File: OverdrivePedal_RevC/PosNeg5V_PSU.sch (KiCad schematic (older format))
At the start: 25 parts, among them U11 TPS60400, U3 TPS60400, U7 SE8233X2, U8 SE8250X2

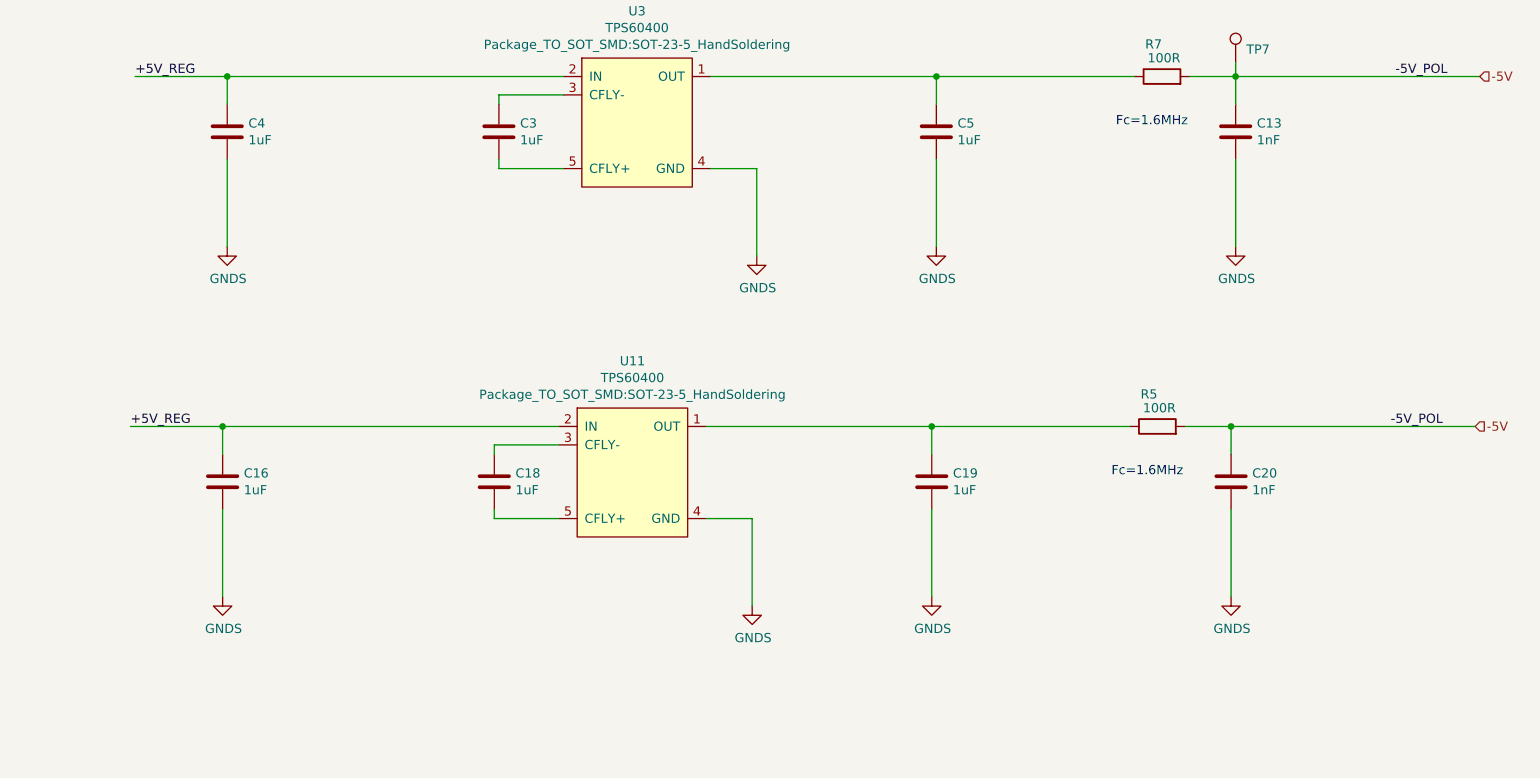
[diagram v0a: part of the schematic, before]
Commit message: updated revc
- Switch PC15 to PA9 for FX_ENABLE
- connected BOOT0 to GND
- Removed U11 charge pump (not required/causing oscillation)
- lowered U3 charge pump LP filter cuttoff to 1.6KHz
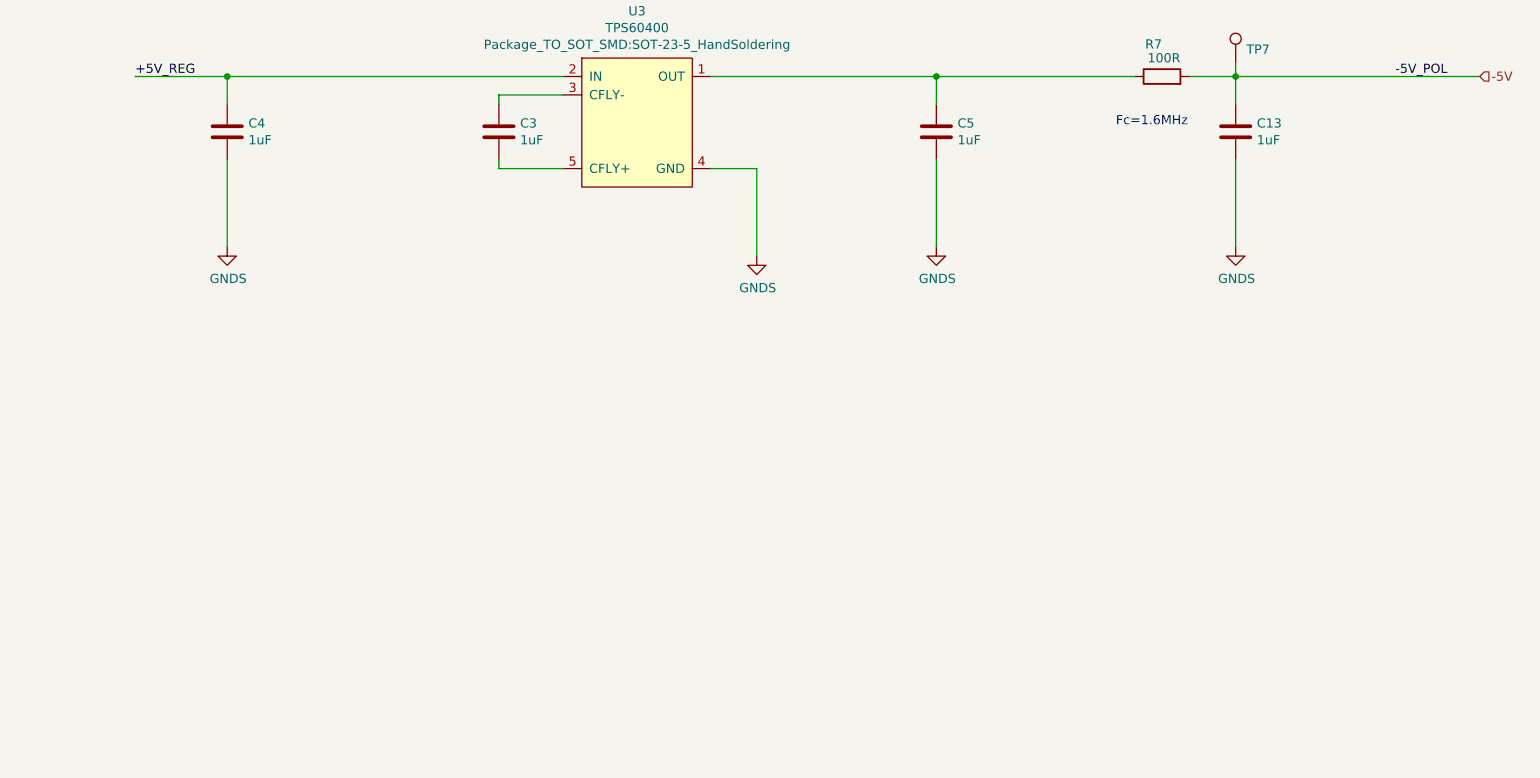
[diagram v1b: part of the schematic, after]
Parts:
- removed C16, C18, C19: 1uF, Capacitor_SMD:C_0402_1005Metric, symbol Device:C
- removed C20: 1nF, Capacitor_SMD:C_0402_1005Metric, symbol Device:C
- removed R5: 100R, Resistor_SMD:R_0402_1005Metric, symbol Device:R
- removed U11: TPS60400, Package_TO_SOT_SMD:SOT-23-5_HandSoldering, symbol TPS6040x:TPS60400
- C13: value 1nF -> 1uF
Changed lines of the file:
@@
 Title "Power Supply"
 Date "2020-03-29"
-Rev "RevB"
+Rev "RevC"
 Comp ""
 Comment1 "U11 may be omitted if U3 can provide enough -5V current"
@@
 AR Path="/5E6A8284/5E8237A8" Ref="C?"  Part="1"
 F 0 "C13" H 10665 5996 50  0000 L CNN
-F 1 "1nF" H 10665 5905 50  0000 L CNN
+F 1 "1uF" H 10665 5905 50  0000 L CNN
 F 2 "Capacitor_SMD:C_0402_1005Metric" H 10588 5800 50  0001 C CNN
 F 3 "~" H 10550 5950 50  0001 C CNN
@@
 -5V
 $Comp
-L power:GNDS #PWR015
-U 1 1 5E82512E
-P 7925 8525
-AR Path="/5E6165F4/5E82512E" Ref="#PWR015"  Part="1"
-AR Path="/5E6A8284/5E82512E" Ref="#PWR?"  Part="1"
-F 0 "#PWR015" H 7925 8275 50  0001 C CNN
-F 1 "GNDS" H 7930 8352 50  0000 C CNN
-F 2 "" H 7925 8525 50  0001 C CNN
-F 3 "" H 7925 8525 50  0001 C CNN
-	1    7925 8525
-	1    0    0    -1
-$EndComp
-Text HLabel 11850 7550 2    50   Input ~ 0
--5V
-$Comp
-L Device:C C18
-U 1 1 5E825135
-P 6525 7850
-AR Path="/5E6165F4/5E825135" Ref="C18"  Part="1"
-AR Path="/5E6A8284/5E825135" Ref="C?"  Part="1"
-F 0 "C18" H 6640 7896 50  0000 L CNN
-F 1 "1uF" H 6640 7805 50  0000 L CNN
-F 2 "Capacitor_SMD:C_0402_1005Metric" H 6563 7700 50  0001 C CNN
-F 3 "~" H 6525 7850 50  0001 C CNN
-	1    6525 7850
-	1    0    0    -1
-$EndComp
-Text Label 4550 7550 0    50   ~ 0
-+5V_REG
-Text Label 11675 7550 2    50   ~ 0
--5V_POL
-$Comp
-L TPS6040x:TPS60400 U?
-U 1 1 5E82513D
-P 7275 7800
-AR Path="/5E82513D" Ref="U?"  Part="1"
-AR Path="/5E6165F4/5E82513D" Ref="U11"  Part="1"
-F 0 "U11" H 7275 8405 50  0000 C CNN
-F 1 "TPS60400" H 7275 8314 50  0000 C CNN
-F 2 "Package_TO_SOT_SMD:SOT-23-5_HandSoldering" H 7275 8223 50  0000 C CNN
-F 3 "http://www.ti.com/lit/ds/symlink/tps60402.pdf" H 7225 7950 50  0001 C CNN
-	1    7275 7800
-	1    0    0    -1
-$EndComp
-Wire Wire Line
-	7675 7550 8900 7550
-Wire Wire Line
-	4550 7550 5050 7550
-Wire Wire Line
-	7925 8050 7925 8525
-Wire Wire Line
-	7925 8050 7675 8050
-Wire Wire Line
-	6525 7700 6525 7650
-Wire Wire Line
-	6525 7650 6875 7650
-Wire Wire Line
-	6875 8050 6525 8050
-Wire Wire Line
-	6525 8050 6525 8000
-$Comp
-L Device:C C16
-U 1 1 5E82514B
-P 5050 7850
-AR Path="/5E6165F4/5E82514B" Ref="C16"  Part="1"
-AR Path="/5E6A8284/5E82514B" Ref="C?"  Part="1"
-F 0 "C16" H 5165 7896 50  0000 L CNN
-F 1 "1uF" H 5165 7805 50  0000 L CNN
-F 2 "Capacitor_SMD:C_0402_1005Metric" H 5088 7700 50  0001 C CNN
-F 3 "~" H 5050 7850 50  0001 C CNN
-	1    5050 7850
-	1    0    0    -1
-$EndComp
-Wire Wire Line
-	5050 7700 5050 7550
-Connection ~ 5050 7550
-Wire Wire Line
-	5050 7550 6875 7550
-$Comp
-L power:GNDS #PWR07
-U 1 1 5E825154
-P 5050 8475
-AR Path="/5E6165F4/5E825154" Ref="#PWR07"  Part="1"
-AR Path="/5E6A8284/5E825154" Ref="#PWR?"  Part="1"
-F 0 "#PWR07" H 5050 8225 50  0001 C CNN
-F 1 "GNDS" H 5055 8302 50  0000 C CNN
-F 2 "" H 5050 8475 50  0001 C CNN
-F 3 "" H 5050 8475 50  0001 C CNN
-	1    5050 8475
-	1    0    0    -1
-$EndComp
-Wire Wire Line
-	5050 8000 5050 8475
-$Comp
-L Device:C C19
-U 1 1 5E82515B
-P 8900 7850
-AR Path="/5E6165F4/5E82515B" Ref="C19"  Part="1"
-AR Path="/5E6A8284/5E82515B" Ref="C?"  Part="1"
-F 0 "C19" H 9015 7896 50  0000 L CNN
-F 1 "1uF" H 9015 7805 50  0000 L CNN
-F 2 "Capacitor_SMD:C_0402_1005Metric" H 8938 7700 50  0001 C CNN
-F 3 "~" H 8900 7850 50  0001 C CNN
-	1    8900 7850
-	1    0    0    -1
-$EndComp
-Wire Wire Line
-	8900 7700 8900 7550
-$Comp
-L power:GNDS #PWR019
-U 1 1 5E825162
-P 8900 8475
-AR Path="/5E6165F4/5E825162" Ref="#PWR019"  Part="1"
-AR Path="/5E6A8284/5E825162" Ref="#PWR?"  Part="1"
-F 0 "#PWR019" H 8900 8225 50  0001 C CNN
-F 1 "GNDS" H 8905 8302 50  0000 C CNN
-F 2 "" H 8900 8475 50  0001 C CNN
-F 3 "" H 8900 8475 50  0001 C CNN
-	1    8900 8475
-	1    0    0    -1
-$EndComp
-Wire Wire Line
-	8900 8000 8900 8475
-Wire Wire Line
-	8900 7550 9975 7550
-Connection ~ 8900 7550
-$Comp
-L Device:C C20
-U 1 1 5E82516B
-P 10525 7850
-AR Path="/5E6165F4/5E82516B" Ref="C20"  Part="1"
-AR Path="/5E6A8284/5E82516B" Ref="C?"  Part="1"
-F 0 "C20" H 10640 7896 50  0000 L CNN
-F 1 "1nF" H 10640 7805 50  0000 L CNN
-F 2 "Capacitor_SMD:C_0402_1005Metric" H 10563 7700 50  0001 C CNN
-F 3 "~" H 10525 7850 50  0001 C CNN
-	1    10525 7850
-	1    0    0    -1
-$EndComp
-Wire Wire Line
-	10525 7700 10525 7550
-$Comp
-L power:GNDS #PWR023
-U 1 1 5E825172
-P 10525 8475
-AR Path="/5E6165F4/5E825172" Ref="#PWR023"  Part="1"
-AR Path="/5E6A8284/5E825172" Ref="#PWR?"  Part="1"
-F 0 "#PWR023" H 10525 8225 50  0001 C CNN
-F 1 "GNDS" H 10530 8302 50  0000 C CNN
-F 2 "" H 10525 8475 50  0001 C CNN
-F 3 "" H 10525 8475 50  0001 C CNN
-	1    10525 8475
-	1    0    0    -1
-$EndComp
-Wire Wire Line
-	10525 8000 10525 8475
-$Comp
-L Device:R R?
-U 1 1 5E825179
-P 10125 7550
-AR Path="/5E825179" Ref="R?"  Part="1"
-AR Path="/5E6165F4/5E825179" Ref="R5"  Part="1"
-F 0 "R5" V 10300 7550 50  0000 L CNN
-F 1 "100R" V 10225 7450 50  0000 L CNN
-F 2 "Resistor_SMD:R_0402_1005Metric" V 10055 7550 50  0001 C CNN
-F 3 "~" H 10125 7550 50  0001 C CNN
-	1    10125 7550
-	0    -1   -1   0
-$EndComp
-Wire Wire Line
-	10275 7550 10525 7550
-Connection ~ 10525 7550
-Wire Wire Line
-	10525 7550 11850 7550
-Text Notes 9875 7825 0    50   ~ 0
-Fc=1.6MHz
-$Comp
 L Connector:TestPoint TP5
